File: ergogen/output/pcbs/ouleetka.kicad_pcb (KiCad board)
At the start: 2 copper layers, 144.6 x 93.8 mm, 65 parts

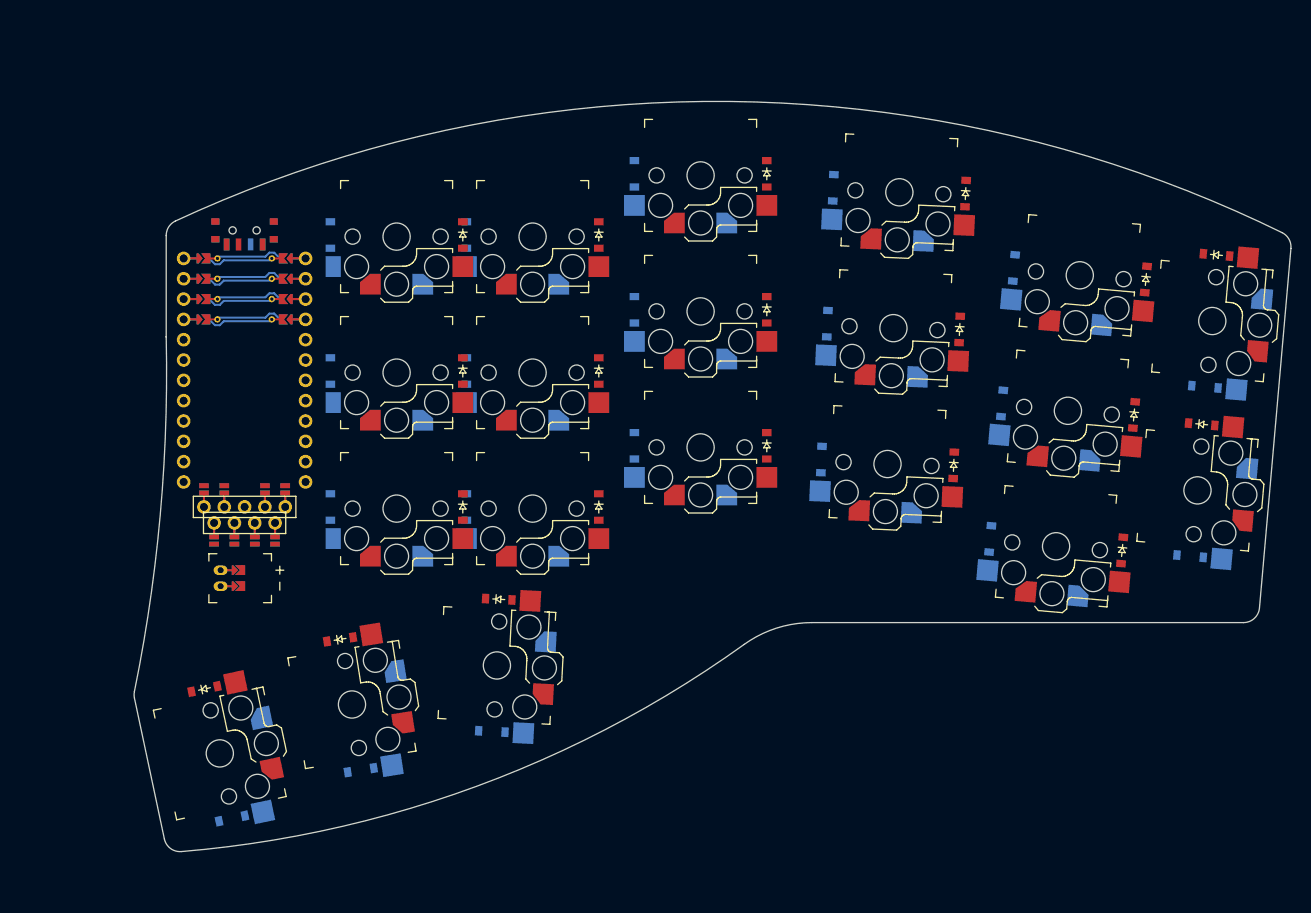
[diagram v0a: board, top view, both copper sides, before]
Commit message: update footprints position
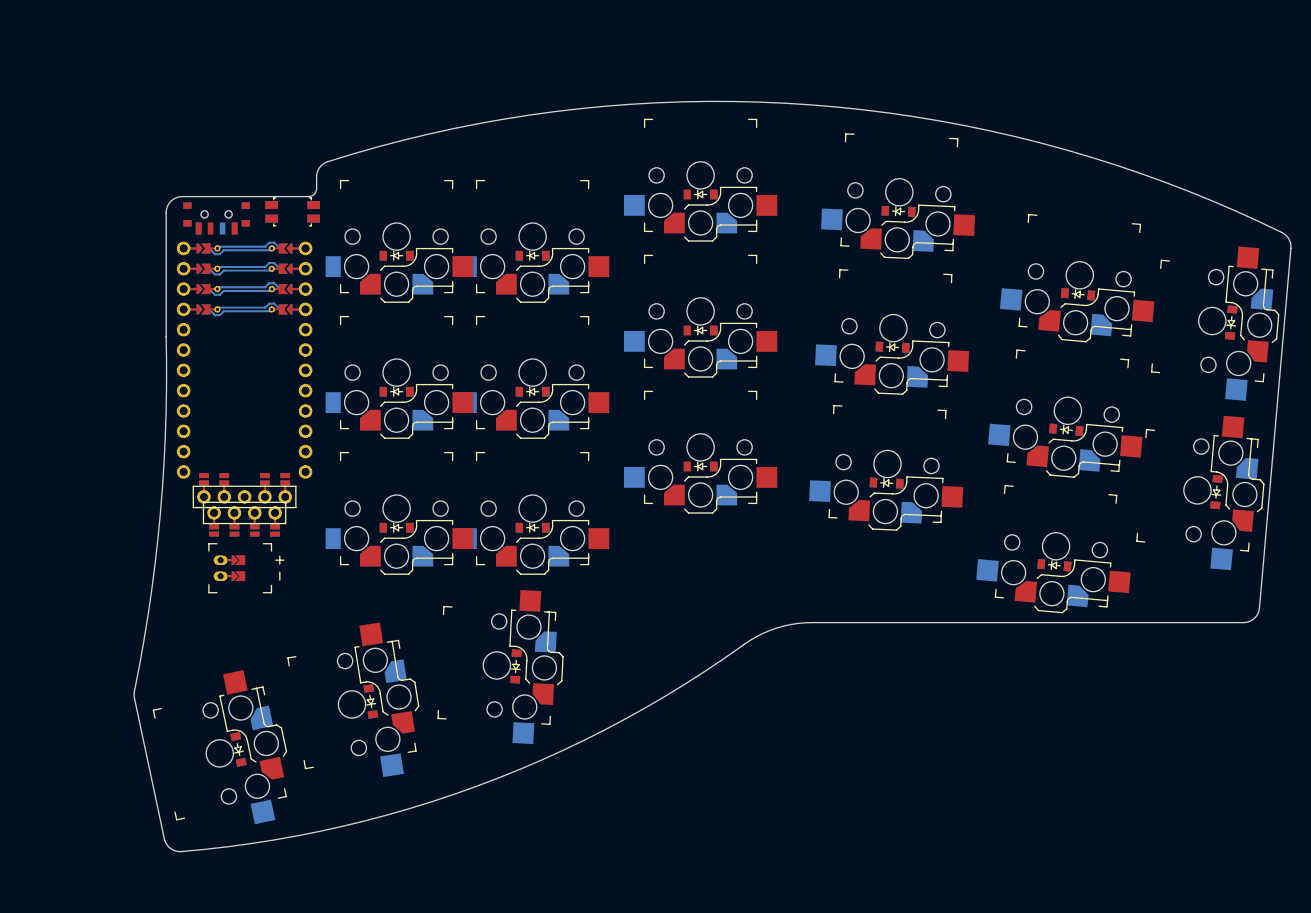
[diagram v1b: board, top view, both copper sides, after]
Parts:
- added RST1: , ceoloide:reset_button_smd_side, F.Cu at (87.0, 62.9)
- PWR1: value power_switch -> (none)
- moved D32 8.67 mm to (162.7, 62.8), turned to 177.5 degrees
- moved D30 8.67 mm to (161.3, 96.8), turned to 177.5 degrees
- moved D31 8.67 mm to (162.0, 79.8), turned to 177.5 degrees
- moved D33 8.67 mm to (182.2, 107.1), turned to 175 degrees
- moved D34 8.67 mm to (183.7, 90.1), turned to 175 degrees
- moved D35 8.67 mm to (185.2, 73.2), turned to 175 degrees
- moved D36 8.67 mm to (202.5, 97.9), turned to 265 degrees
- moved D37 8.67 mm to (204.3, 76.8), turned to 265 degrees
- moved D20 8.67 mm to (114.9, 119.7), turned to 87 degrees
- moved D18 8.67 mm to (80.2, 130.1), turned to 102 degrees
- moved D1 8.67 mm to (100.0, 102.4), turned to 0 degrees
- moved D2 8.67 mm to (100.0, 85.4), turned to 0 degrees
- moved D21 8.67 mm to (100.0, 102.4), turned to 180 degrees
- moved D22 8.67 mm to (100.0, 85.4), turned to 180 degrees
- moved D23 8.67 mm to (100.0, 68.4), turned to 180 degrees
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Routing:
- net (no net): track 0.00 -> 112.6 mm
- net inner_top: track 33.9 -> 0.00 mm
- net index_bottom: track 33.8 -> 0.00 mm
- net outer_thome: track 17.0 -> 0.00 mm
- net outer_home: track 17.0 -> 0.00 mm
- net C4: track 5.50 -> 0.00 mm
- net C1: track 5.50 -> 0.00 mm
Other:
- outline, holes or cut-outs redrawn

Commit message: refactoring
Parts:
- moved DISP1 1.77 mm to (81.2, 80.1)
- moved DISP2 1.77 mm to (81.2, 82.1)
- moved JST1 1.27 mm to (78.2, 106.2)
- moved MCU1 1.27 mm to (81.2, 78.9)
- moved PWR1 1.27 mm to (77.8, 62.0)
- moved RST1 1.27 mm to (87.2, 61.7)
- moved D13 0.52 mm to (182.6, 107.5)
- moved D16 0.52 mm to (202.8, 98.3)
- moved D17 0.52 mm to (204.7, 77.2)
- moved D33 0.52 mm to (182.6, 107.5)
- moved D36 0.52 mm to (202.8, 98.3)
- moved D37 0.52 mm to (204.7, 77.2)
- moved S10 0.52 mm to (182.8, 105.1)
- moved S16 0.52 mm to (200.5, 98.1)
- moved S17 0.52 mm to (202.3, 76.9)
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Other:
- board size 144.6 x 93.8 mm -> 145 x 93.8 mm

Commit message: outlines refactoring
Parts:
- moved DISP1 2.60 mm to (81.2, 82.7)
- moved DISP2 2.60 mm to (81.2, 84.7)
- moved MCU1 1.60 mm to (81.2, 80.5)
- moved RST1 1.40 mm to (87.2, 63.1)
- moved PWR1 1.10 mm to (77.8, 63.1)
- moved JST1 0.90 mm to (77.4, 105.8)
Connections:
- net inner_thome renamed inner_default
- net middle_thome renamed middle_default
- net outer_thome renamed outer_default
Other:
- board size 145 x 93.8 mm -> 120.2 x 64.9 mm

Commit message: more changes
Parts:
- removed DISP1: , ceoloide:display_nice_view
- removed DISP2: , ceoloide:display_ssd1306
- removed JST1: , ceoloide:battery_connector_jst_ph_2
- removed MCU1: , ceoloide:mcu_nice_nano
- removed PWR1: , ceoloide:power_switch_smd_side
- removed RST1: , ceoloide:reset_button_smd_side
- S1, S10, S11, S12, S13, S14, S15, S16, S17, S18, S19, S2, S20, S3, S4, S5, S6, S7, S8, S9: moved to B.Cu
- moved S18 131.6 mm to (198.1, 77.0), turned to 85 degrees
- moved S10 91.6 mm to (100.0, 66.0), turned to 180 degrees
- moved S9 66.8 mm to (100.0, 83.0), turned to 180 degrees
- moved S8 66.1 mm to (100.0, 100.0), turned to 180 degrees
- moved S15 60.1 mm to (159.0, 77.6), turned to 177.5 degrees
- moved S14 59.4 mm to (158.2, 94.6), turned to 177.5 degrees
- moved S16 55.4 mm to (159.7, 60.6), turned to 177.5 degrees
- moved S13 55.1 mm to (136.4, 58.6)
- moved S7 52.7 mm to (113.8, 117.1), turned to 266 degrees
- moved S12 49.6 mm to (136.4, 75.6), turned to 180 degrees
- moved S11 48.1 mm to (136.4, 92.6), turned to 180 degrees
- moved S6 45.1 mm to (181.7, 69.3), turned to 175 degrees
- moved S5 43.6 mm to (180.2, 86.2), turned to 175 degrees
- moved S4 42.2 mm to (178.7, 103.1), turned to 175 degrees
- moved S17 22.5 mm to (196.2, 98.6), turned to 85 degrees
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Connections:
- S1 pad : (no net) -> GND
- S1 pad 1: C4 -> index
- S1 pad 2: index_bottom -> bottom
- S10 pad : (no net) -> GND
- S10 pad 1: C1 -> inner
- S10 pad 2: pinky_bottom -> top
- S11 pad : (no net) -> GND
- S11 pad 1: C1 -> middle
- S11 pad 2: pinky_home -> bottom
- S12 pad : (no net) -> GND
- S12 pad 1: C1 -> middle
- S12 pad 2: pinky_top -> home
- S13 pad : (no net) -> GND
- S13 pad 1: C5 -> middle
- S13 pad 2: inner_bottom -> top
- S14 pad : (no net) -> GND
- S14 pad 1: C5 -> ring
- S14 pad 2: inner_home -> bottom
- S15 pad : (no net) -> GND
- S15 pad 1: C5 -> ring
- S15 pad 2: inner_top -> home
- S16 pad : (no net) -> GND
- S16 pad 1: C0 -> ring
- S16 pad 2: outer_bottom -> top
- S17 pad : (no net) -> GND
- S17 pad 1: C0 -> outer
- S17 pad 2: outer_home -> bottom
- S18 pad : (no net) -> GND
- S18 pad 1: C5 -> outer
- S18 pad 2: outer_default -> home
- S19 pad : (no net) -> GND
- S19 pad 1: C4 -> outer
- S19 pad 2: middle_default -> default
- S2 pad : (no net) -> GND
- S2 pad 1: C4 -> index
- S2 pad 2: index_home -> home
- S20 pad : (no net) -> GND
- S20 pad 1: C3 -> middle
- S20 pad 2: inner_default -> default
- S3 pad : (no net) -> GND
- S3 pad 1: C4 -> index
- S3 pad 2: index_top -> top
- S4 pad : (no net) -> GND
- S4 pad 1: C3 -> pinky
- S4 pad 2: middle_bottom -> bottom
- S5 pad : (no net) -> GND
- S5 pad 1: C3 -> pinky
- S5 pad 2: middle_home -> home
- S6 pad : (no net) -> GND
- S6 pad 1: C3 -> pinky
- S6 pad 2: middle_top -> top
- S7 pad : (no net) -> GND
- S7 pad 1: C2 -> inner
- S7 pad 2: ring_bottom -> default
- S8 pad : (no net) -> GND
- S8 pad 1: C2 -> inner
- S8 pad 2: ring_home -> bottom
- S9 pad : (no net) -> GND
- S9 pad 1: C2 -> inner
- S9 pad 2: ring_top -> home
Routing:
- net (no net): track 112.6 -> 0.00 mm
- net GND: track 7.00 -> 0.00 mm
- net JST1_2: track 3.60 -> 0.00 mm
- net JST1_1: track 3.60 -> 0.00 mm
- net VCC: track 3.50 -> 0.00 mm
- net SDA: track 3.50 -> 0.00 mm
- net SCL: track 3.50 -> 0.00 mm
- net SCK: track 3.50 -> 0.00 mm
- net MOSI: track 3.50 -> 0.00 mm
- net CS: track 3.50 -> 0.00 mm
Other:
- board size 120.2 x 64.9 mm -> 155 x 110 mm

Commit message: more changes
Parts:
- removed D21, D22, D23, D24, D25, D26, D27, D28, D29, D30, D31, D32, D33, D34, D35, D36, D37, D38, D39, D40: , ceoloide:diode_tht_sod123
- added DISP1: , ceoloide:display_nice_view, F.Cu at (81.8, 81.8)
- added DISP2: , ceoloide:display_ssd1306, F.Cu at (81.8, 83.8)
- added H1: , ceoloide:mounting_hole_plated, F.Cu at (108.5, 58.0)
- added H10: , ceoloide:mounting_hole_plated, F.Cu at (192.4, 87.1)
- added H2: , ceoloide:mounting_hole_plated, F.Cu at (107.0, 127.5)
- added H3: , ceoloide:mounting_hole_plated, F.Cu at (150.4, 56.1)
- added H4: , ceoloide:mounting_hole_plated, F.Cu at (150.4, 107.9)
- added H5: , ceoloide:mounting_hole_plated, F.Cu at (205.1, 68.2)
- added H6: , ceoloide:mounting_hole_plated, F.Cu at (74.3, 101.9)
- added H7: , ceoloide:mounting_hole_plated, F.Cu at (201.6, 107.9)
- added H8: , ceoloide:mounting_hole_plated, F.Cu at (86.5, 120.6)
- added H9: , ceoloide:mounting_hole_plated, F.Cu at (130.1, 84.1)
- added JST1: , ceoloide:battery_connector_jst_ph_2, F.Cu at (84.8, 106.8)
- added LED1: , ceoloide:led_SK6812mini-e (underglow, reversible), B.Cu at (100.0, 78.0)
- added LED2: , ceoloide:led_SK6812mini-e (underglow, reversible), B.Cu at (138.4, 70.6)
- added LED3: , ceoloide:led_SK6812mini-e (underglow, reversible), B.Cu at (183.7, 81.2)
- added LED4: , ceoloide:led_SK6812mini-e (underglow, reversible), B.Cu at (75.2, 131.6)
- added LED5: , ceoloide:led_SK6812mini-e (underglow, reversible), B.Cu at (91.4, 123.3)
- added MCU1: , ceoloide:mcu_nice_nano, F.Cu at (81.8, 78.9)
- added PWR1: , ceoloide:power_switch_smd_side, F.Cu at (81.8, 62.6)
- added RST1: , ceoloide:reset_switch_tht_top, F.Cu at (80.0, 112.0)
- added S21: , ceoloide:switch_choc_v1_v2, B.Cu at (80.0, 130.2)
- added S22: , ceoloide:switch_choc_v1_v2, B.Cu at (96.3, 122.5)
- moved D18 113.4 mm to (186.9, 85.8), turned to -95 degrees
- moved D16 91.6 mm to (103.6, 82.2), turned to -90 degrees
- moved D15 85.7 mm to (108.7, 116.8), turned to 266 degrees
- moved S18 59.7 mm to (138.4, 75.6), turned to 180 degrees
- moved S16 54.8 mm to (199.2, 98.6), turned to 85 degrees
- moved D17 53.8 mm to (142.0, 74.8), turned to -90 degrees
- moved S13 43.8 mm to (161.2, 94.6), turned to 177.5 degrees
- moved D10 41.8 mm to (162.9, 55.5), turned to 177.5 degrees
- moved D7 41.6 mm to (138.4, 53.4), turned to 180 degrees
- moved D3 31.5 mm to (117.0, 94.8), turned to 180 degrees
- moved D11 29.5 mm to (182.2, 98.0), turned to 175 degrees
- moved D6 28.6 mm to (138.4, 87.4), turned to 180 degrees
- moved D14 28.5 mm to (206.2, 77.4), turned to 85 degrees
- moved D9 28.3 mm to (162.2, 72.5), turned to 177.5 degrees
- moved D8 27.6 mm to (161.5, 89.5), turned to 177.5 degrees
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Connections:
- net pinky renamed C1
- D1 pad 2: inner_bottom -> R2S
- D10 pad 1: R2 -> R0
- D10 pad 2: ring_bottom -> R0S
- D11 pad 1: R1 -> R2
- D11 pad 2: ring_home -> R2S
- D12 pad 2: ring_top -> R0S
- D13 pad 2: pinky_bottom -> R2S
- D14 pad 2: pinky_home -> R1S
- D15 pad 1: R0 -> R3
- D15 pad 2: pinky_top -> R3S
- D16 pad 1: R2 -> R1
- D16 pad 2: outer_bottom -> R1S
- D17 pad 2: outer_home -> R1S
- D18 pad 1: R3 -> R1
- D18 pad 2: outer_default -> R1S
- D19 pad 2: middle_default -> R3S
- D2 pad 1: R1 -> R0
- D2 pad 2: inner_home -> R0S
- D20 pad 2: inner_default -> R3S
- D3 pad 1: R0 -> R2
- D3 pad 2: inner_top -> R2S
- D4 pad 1: R2 -> R1
- D4 pad 2: index_bottom -> R1S
- D5 pad 1: R1 -> R0
- D5 pad 2: index_home -> R0S
- D6 pad 1: R0 -> R2
- D6 pad 2: index_top -> R2S
- D7 pad 1: R2 -> R0
- D7 pad 2: middle_bottom -> R0S
- D8 pad 1: R1 -> R2
- D8 pad 2: middle_home -> R2S
- D9 pad 1: R0 -> R1
- D9 pad 2: middle_top -> R1S
- S1 pad : GND -> R2
- S1 pad 1: index -> C4
- S1 pad 2: bottom -> R2S
- S10 pad : GND -> DOUT
- S10 pad 1: inner -> C5
- S10 pad 2: top -> R1S
- S11 pad : GND -> R2
- S11 pad 1: middle -> C3
- S11 pad 2: bottom -> R2S
- S12 pad : GND -> R0
- S12 pad 1: middle -> C3
- S12 pad 2: home -> R0S
- S13 pad : GND -> R2
- S13 pad 1: middle -> C2
- S13 pad 2: top -> R2S
- S14 pad : GND -> R1
- S14 pad 1: ring -> C2
- S14 pad 2: bottom -> R1S
- S15 pad : GND -> R0
- S15 pad 1: ring -> C2
- S15 pad 2: home -> R0S
- S16 pad : GND -> R2
- S16 pad 1: ring -> C0
- S16 pad 2: top -> R2S
- S17 pad : GND -> R1
- S17 pad 1: outer -> C0
- S17 pad 2: bottom -> R1S
- S18 pad : GND -> DOUT
- S18 pad 1: outer -> C3
- S18 pad 2: home -> R1S
- S19 pad : GND -> DOUT
- S19 pad 1: outer -> C5
- S19 pad 2: default -> R3S
- S2 pad : GND -> R1
- S2 pad 1: index -> C4
- S2 pad 2: home -> R1S
- S20 pad : GND -> DOUT
- S20 pad 1: middle -> C4
- S20 pad 2: default -> R3S
- S3 pad : GND -> R0
- S3 pad 1: index -> C4
- S3 pad 2: top -> R0S
- S4 pad : GND -> R2
- S4 pad 2: bottom -> R2S
- S5 pad : GND -> R1
- S5 pad 2: home -> R1S
- S6 pad : GND -> R0
- S6 pad 2: top -> R0S
- S7 pad : GND -> R3
- S7 pad 1: inner -> C3
- S7 pad 2: default -> R3S
- S8 pad : GND -> R2
- S8 pad 1: inner -> C5
- S8 pad 2: bottom -> R2S
- S9 pad : GND -> R0
- S9 pad 1: inner -> C5
- S9 pad 2: home -> R0S
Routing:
- net (no net): track 0.00 -> 112.6 mm
- net GND: track 0.00 -> 7.00 mm
- net JST1_2: track 0.00 -> 3.60 mm
- net JST1_1: track 0.00 -> 3.60 mm
- net VCC: track 0.00 -> 3.50 mm
- net SDA: track 0.00 -> 3.50 mm
- net SCL: track 0.00 -> 3.50 mm
- net SCK: track 0.00 -> 3.50 mm
- net MOSI: track 0.00 -> 3.50 mm
- net CS: track 0.00 -> 3.50 mm
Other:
- board size 155 x 110 mm -> 158 x 110 mm

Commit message: more changes
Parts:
- removed H1, H10, H2, H3, H4, H5, H6, H7, H8, H9: , ceoloide:mounting_hole_plated
- removed S21, S22: , ceoloide:switch_choc_v1_v2
- added MH1: , ceoloide:mounting_hole_plated, F.Cu at (108.5, 58.0)
- added MH2: , ceoloide:mounting_hole_plated, F.Cu at (107.0, 127.5)
- added MH3: , ceoloide:mounting_hole_plated, F.Cu at (150.4, 56.1)
- added MH4: , ceoloide:mounting_hole_plated, F.Cu at (150.4, 107.9)
- added MH5: , ceoloide:mounting_hole_plated, F.Cu at (205.1, 68.2)
- added MH6: , ceoloide:mounting_hole_plated, F.Cu at (74.3, 101.9)
- added MH7: , ceoloide:mounting_hole_plated, F.Cu at (201.6, 107.9)
- added SH1: , ceoloide:mounting_hole_npth, F.Cu at (86.0, 119.7)
- added SH2: , ceoloide:mounting_hole_npth, F.Cu at (129.6, 84.1)
- added SH3: , ceoloide:mounting_hole_npth, F.Cu at (192.6, 86.5)
- moved S9 53.0 mm to (113.8, 117.1), turned to 356 degrees
- moved S8 34.0 mm to (100.0, 66.0)
- moved S7 22.0 mm to (100.0, 100.0), turned to 180 degrees
- moved JST1 11.5 mm to (73.3, 107.0), turned to 90 degrees
- moved D15 7.28 mm to (113.5, 122.3), turned to 356 degrees
- moved RST1 3.26 mm to (76.8, 112.2), turned to 0 degrees
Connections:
- net P9 renamed MCU1_12
- DISP1 pad 16: SCK -> SCL
- DISP1 pad 17: MOSI -> SDA
- DISP1 pad 26: SCK -> SCL
- DISP1 pad 27: MOSI -> SDA
- JST1 pad 1: BAT+ -> BAT_P
- MCU1 pad 10: R2 -> MCU1_10
- MCU1 pad 11: R3 -> MCU1_11
- MCU1 pad 13: P10 -> MCU1_13
- MCU1 pad 14: P16 -> MCU1_14
- MCU1 pad 15: C5 -> MCU1_15
- MCU1 pad 16: C4 -> MCU1_16
- MCU1 pad 17: C3 -> MCU1_17
- MCU1 pad 18: C2 -> MCU1_18
- MCU1 pad 19: C1 -> MCU1_19
- MCU1 pad 20: C0 -> MCU1_20
- MCU1 pad 5: SDA -> MCU1_5
- MCU1 pad 6: SCL -> MCU1_6
- MCU1 pad 7: CS -> MCU1_7
- MCU1 pad 8: R0 -> MCU1_8
- MCU1 pad 9: R1 -> MCU1_9
- S7 pad : R3 -> R2
- S7 pad 1: C3 -> C5
- S7 pad 2: R3S -> R2S
- S8 pad : R2 -> R0
- S8 pad 2: R2S -> R0S
- S9 pad : R0 -> R3
- S9 pad 1: C5 -> C3
- S9 pad 2: R0S -> R3S
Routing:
- net (no net): track 112.6 -> 337.7 mm
- net SDA: track 3.50 -> 7.00 mm
- net SCL: track 3.50 -> 7.00 mm
- net SCK: track 3.50 -> 0.00 mm
- net MOSI: track 3.50 -> 0.00 mm
- added copper zone on B.Cu, net GND
- added copper zone on F.Cu, net GND
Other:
- board size 158 x 110 mm -> 141 x 92.9 mm

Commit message: more changes
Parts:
- RST1: footprint ceoloide:reset_switch_tht_top -> ceoloide:reset_switch_smd_side
- moved S6 90.1 mm to (100.0, 100.0), turned to 180 degrees
- moved S10 83.3 mm to (183.2, 86.2), turned to 175 degrees
- moved S8 53.0 mm to (113.8, 117.1), turned to -4 degrees
- moved RST1 51.0 mm to (88.3, 62.6)
- moved S9 36.8 mm to (100.0, 83.0), turned to 180 degrees
- moved S7 34.0 mm to (100.0, 66.0)
- moved S5 17.0 mm to (184.7, 69.3)
- moved PWR1 2.52 mm to (79.3, 62.3)
- moved JST1 0.25 mm to (73.3, 107.2)
- moved DISP1 0.10 mm to (81.8, 81.9)
- moved DISP2 0.10 mm to (81.8, 83.9)
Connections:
- LED1 pad 2: DOUT -> LED1_1
- LED1 pad 4: DIN -> LED1
- LED2 pad 2: DOUT -> LED1_2
- LED2 pad 4: DIN -> LED1_1
- LED3 pad 2: DOUT -> LED1_3
- LED3 pad 4: DIN -> LED1_2
- LED4 pad 2: DOUT -> LED0_1
- LED4 pad 4: DIN -> LED0
- LED5 pad 2: DOUT -> LED0_2
- LED5 pad 4: DIN -> LED0_1
- RST1 pad 1: RST -> GND
- RST1 pad 2: GND -> RST
- S1 pad : R2 -> R2S
- S10 pad : DOUT -> LED1_2
- S10 pad 1: C5 -> C1
- S11 pad : R2 -> R2S
- S12 pad : R0 -> R0S
- S13 pad : R2 -> R2S
- S14 pad : R1 -> R1S
- S15 pad : R0 -> R0S
- S16 pad : R2 -> R2S
- S17 pad : R1 -> R1S
- S18 pad : DOUT -> LED1_1
- S19 pad : DOUT -> LED0
- S2 pad : R1 -> R1S
- S20 pad : DOUT -> LED0_1
- S3 pad : R0 -> R0S
- S4 pad : R2 -> R2S
- S5 pad : R1 -> R0S
- S5 pad 2: R1S -> R0S
- S6 pad : R0 -> R2S
- S6 pad 1: C1 -> C5
- S6 pad 2: R0S -> R2S
- S7 pad : R2 -> R0S
- S7 pad 2: R2S -> R0S
- S8 pad : R0 -> R3S
- S8 pad 1: C5 -> C3
- S8 pad 2: R0S -> R3S
- S9 pad : R3 -> LED1
- S9 pad 1: C3 -> C5
- S9 pad 2: R3S -> R1S
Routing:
- net (no net): track 337.7 -> 0.00 mm
- net R0: track 0.00 -> 163.5 mm
- net R0S: track 0.00 -> 68.5 mm
- net GND: track 7.00 -> 29.5 mm
- net R1S: track 0.00 -> 13.7 mm
- net R1: track 0.00 -> 13.2 mm
- net RST: track 0.00 -> 9.84 mm
- net RAW: track 0.00 -> 9.84 mm
- net P10: track 0.00 -> 9.84 mm
- net C5: track 0.00 -> 9.84 mm
- net C3: track 0.00 -> 9.84 mm
- net C1: track 0.00 -> 9.84 mm
- net P16: track 0.00 -> 9.84 mm
- net C4: track 0.00 -> 9.84 mm
- net C2: track 0.00 -> 9.84 mm
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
